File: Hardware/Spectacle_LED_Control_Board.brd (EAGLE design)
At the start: 25.4 x 55.9 mm, 43 parts, among them J3 USB-MICROB, J4 AUDIO-JACK3, J8 AUDIO-JACK3, U1 CY8C4146LQI-S422, U2 3.3V, U4 SN74LVC1G66, U5 SN74LVC1G66

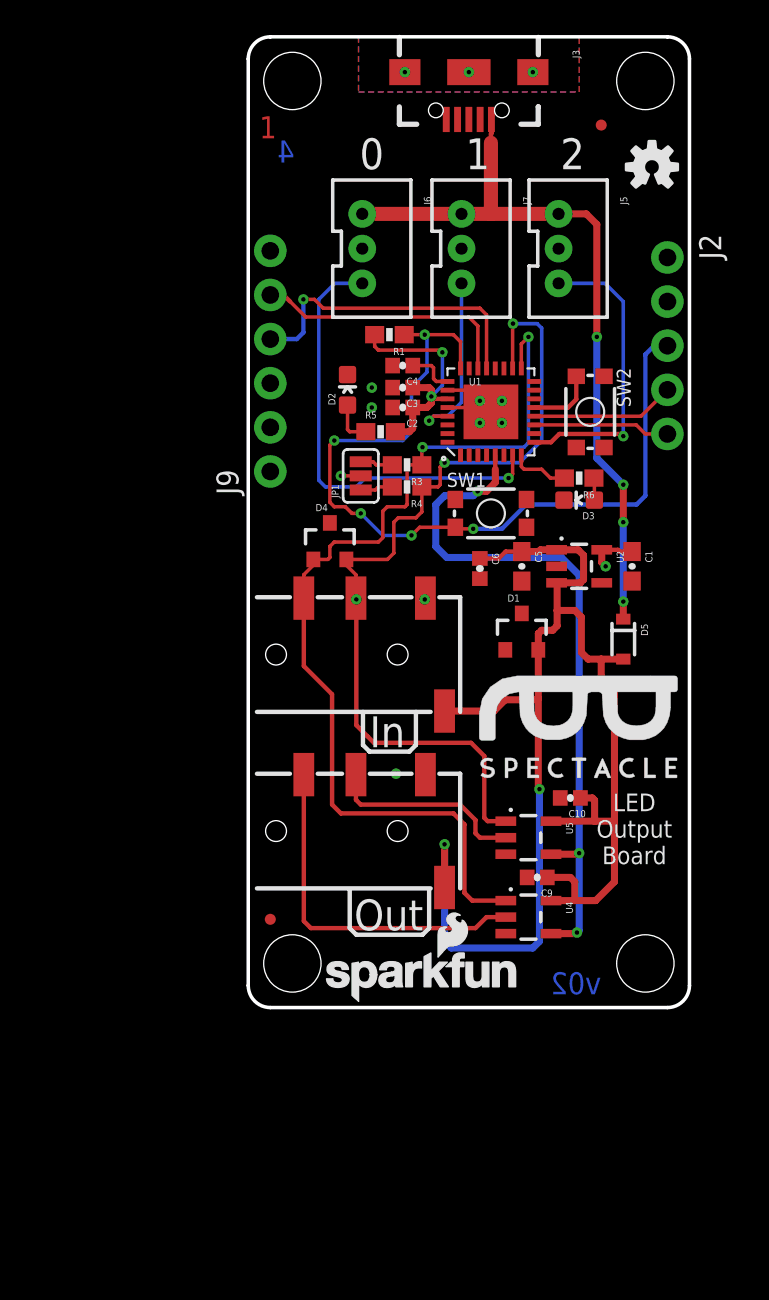
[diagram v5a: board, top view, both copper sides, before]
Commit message: Primarily for changing to PSOC4245LQI-483 Interstitial commit for firmware
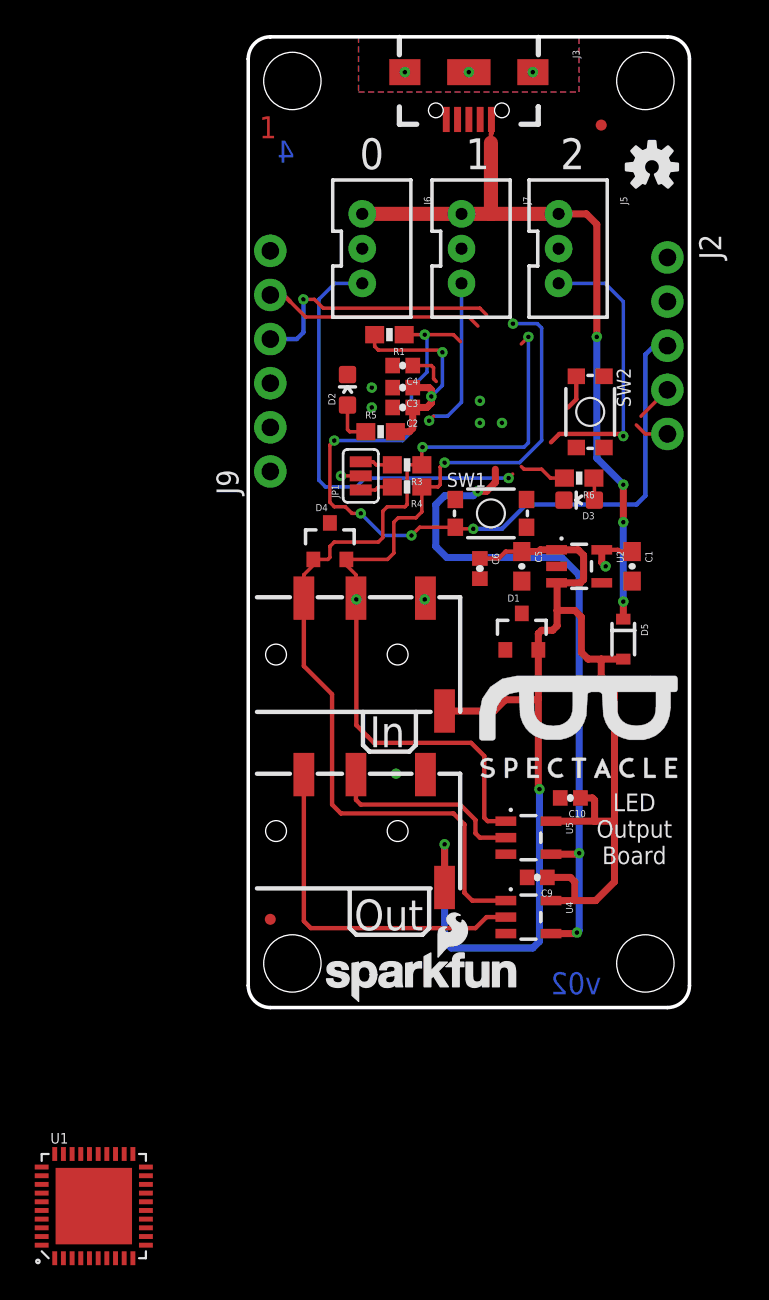
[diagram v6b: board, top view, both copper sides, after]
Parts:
- U1: value CY8C4146LQI-S422 -> CY8C4245LQI-483; device SparkFun-DigitalIC:QFN-32 -> SparkFun-IC-Microcontroller:QFN-40
- moved U1 51.1 mm to (-8.89, -11.4)
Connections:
- net 3.3V: now also U1.32, U1.33; no longer U1.27
- net BTN: now also U1.38; no longer U1.13
- net GND: now also U1.34, U1.9; no longer U1.26, U1.28
- net I2C_OUT_EN: now also U1.4; no longer U1.5
- net LED: now also U1.39; no longer U1.8
- net LED_0: now also U1.10; no longer U1.9
- net RXI: now also U1.26; no longer U1.21
- net SCL: now also U1.18; no longer U1.17
- net SDA: now also U1.19; no longer U1.18
- net SWD_CLK: now also U1.13; no longer U1.12
- net SWD_DATA: now also U1.12; no longer U1.11
- net TXO: now also U1.27; no longer U1.22
- net VCC: now also U1.31; no longer U1.25
- net XRES: now also U1.30; no longer U1.24
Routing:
- net GND: track 6.52 -> 0.00 mm, vias 8 -> 7
- net SWD_CLK: track 8.29 -> 2.15 mm
- net SWD_DATA: track 7.88 -> 2.01 mm
- net RXI: track 18.0 -> 14.9 mm
- net SDA: track 50.1 -> 47.6 mm
- net TXO: track 15.1 -> 12.7 mm
- net BTN: track 3.94 -> 2.00 mm
- net XRES: track 48.9 -> 47.3 mm
- net SCL: track 56.0 -> 54.6 mm
- net I2C_OUT_EN: track 41.2 -> 39.9 mm
- net LED_1: track 26.0 -> 24.9 mm
- net LED_0: track 17.3 -> 16.3 mm
- net 3.3V: track 17.8 -> 16.9 mm
- net LED_2: track 10.3 -> 9.51 mm
- net VCC: track 2.75 -> 2.10 mm
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
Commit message: routing redesign with new processor
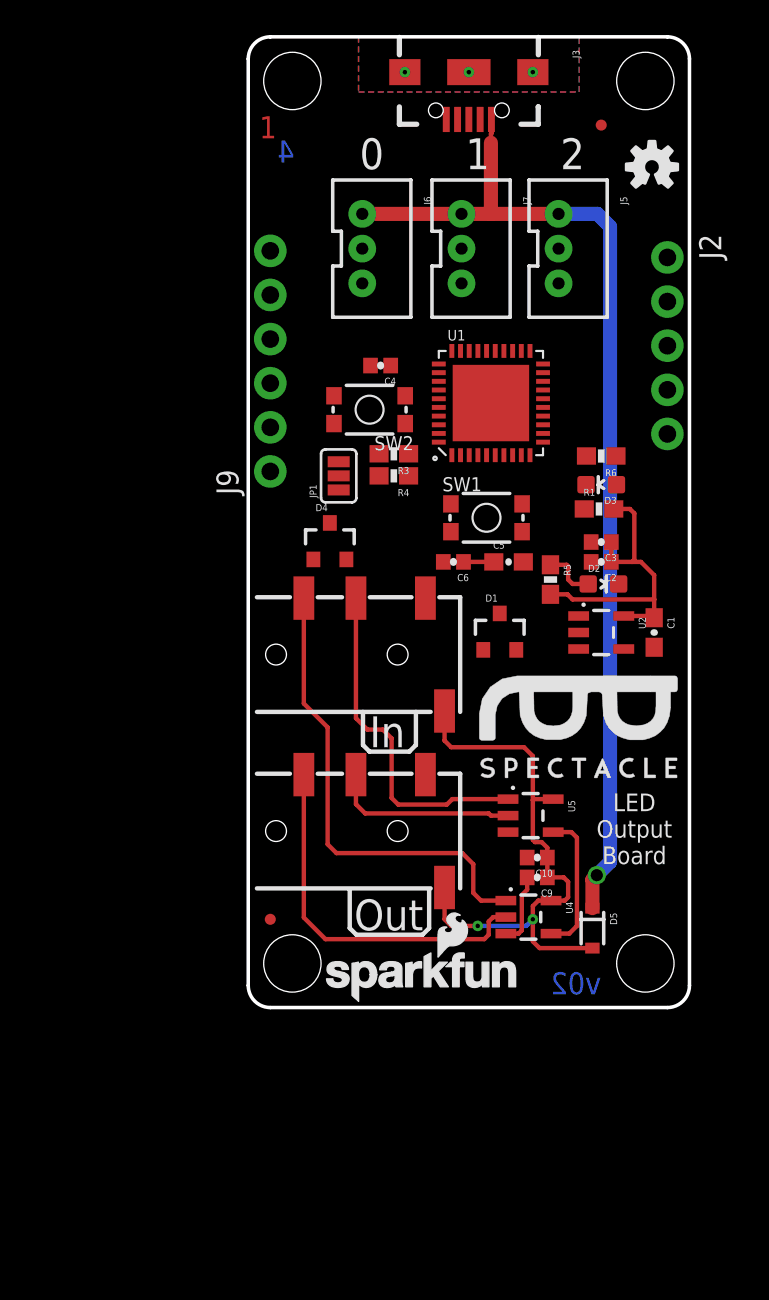
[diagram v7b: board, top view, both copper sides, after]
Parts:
- moved U1 51.6 mm to (14.0, 34.8)
- moved D2 18.5 mm to (20.4, 24.4), turned to 270 degrees
- moved D5 16.7 mm to (19.8, 4.57)
- moved R1 15.7 mm to (20.2, 28.7), turned to 0 degrees
- moved C2 14.5 mm to (20.3, 25.7)
- moved C3 14.5 mm to (20.3, 26.8)
- moved R5 13.0 mm to (17.4, 24.6), turned to 270 degrees
- moved SW2 12.7 mm to (6.99, 34.4), turned to 180 degrees
- moved C1 4.02 mm to (23.4, 21.6)
- moved U2 4.02 mm to (20.3, 21.6)
- moved C10 3.92 mm to (16.6, 8.64)
- moved R6 1.80 mm to (20.3, 31.8)
- moved C6 1.57 mm to (11.8, 25.7), turned to 180 degrees
- moved D3 1.55 mm to (20.3, 30.1)
- moved U5 1.28 mm to (16.3, 11.0)
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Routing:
- net VIN: track 82.3 -> 34.9 mm
- net XRES: track 47.3 -> 0.00 mm, vias 5 -> 0
- net I2C_OUT_EN: track 39.9 -> 8.26 mm, vias 3 -> 0
- net SDA: track 47.6 -> 19.9 mm, vias 3 -> 0
- net SCL: track 54.6 -> 27.3 mm, vias 2 -> 0
- net LED_1: track 24.9 -> 0.00 mm, vias 1 -> 0
- net 5V: track 42.6 -> 59.7 mm, vias 4 -> 1
- net LED_0: track 16.3 -> 0.00 mm, vias 1 -> 0
- net RXI: track 14.9 -> 0.00 mm, vias 1 -> 0
- net TXO: track 12.7 -> 0.00 mm
- net LED_2: track 9.51 -> 0.00 mm, vias 1 -> 0
- net GND: track 0.00 -> 4.17 mm, vias 7 -> 0
- net LED: track 2.75 -> 0.00 mm
- net SWD_CLK: track 2.15 -> 0.00 mm
- net VCC: track 2.10 -> 0.00 mm
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
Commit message: Routing!
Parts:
- moved JP1 11.5 mm to (16.5, 28.4), turned to 270 degrees
- moved SW1 8.24 mm to (6.48, 32.1), turned to 180 degrees
- moved R3 6.30 mm to (13.1, 27.7), turned to 0 degrees
- moved R4 4.71 mm to (13.0, 29.5), turned to 0 degrees
- moved D4 3.58 mm to (7.87, 28.4), turned to 90 degrees
- moved SW2 1.37 mm to (6.48, 35.7)
- moved C4 1.25 mm to (7.11, 38.1)
- moved C2 1.20 mm to (21.0, 26.7), turned to 270 degrees
- moved C3 0.65 mm to (19.7, 26.7), turned to 270 degrees
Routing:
- net GND: track 4.17 -> 44.9 mm, vias 0 -> 2
- net SCL: track 27.3 -> 58.4 mm, vias 0 -> 2
- net SDA: track 19.9 -> 50.1 mm, vias 0 -> 4
- net I2C_OUT_EN: track 8.26 -> 37.0 mm, vias 0 -> 2
- net XRES: track 0.00 -> 24.8 mm, vias 0 -> 4
- net 3.3V: track 18.4 -> 41.6 mm, vias 0 -> 1
- net VIN: track 34.9 -> 54.9 mm
- net LED_1: track 0.00 -> 19.5 mm, vias 0 -> 2
- net TXO: track 0.00 -> 14.3 mm, vias 0 -> 1
- net RXI: track 0.00 -> 14.1 mm, vias 0 -> 2
- net LED_0: track 0.00 -> 13.3 mm, vias 0 -> 1
- net SWD_CLK: track 0.00 -> 8.29 mm
- net SWD_DATA: track 0.00 -> 7.17 mm, vias 0 -> 1
- net BTN: track 0.00 -> 4.85 mm
- net LED_2: track 0.00 -> 3.91 mm
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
